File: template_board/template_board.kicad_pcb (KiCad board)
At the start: 4 copper layers, 90.2 x 95.9 mm, 123 parts, among them J1 USB_C_Receptacle_USB2.0_16P, J4 SWD, M1 MountingHole, M2 MountingHole, M3 MountingHole, M4 MountingHole, Q2 MMST3904, Q3 AO3400A, SW1 SW_Push, SW2 SW_DIP_x01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

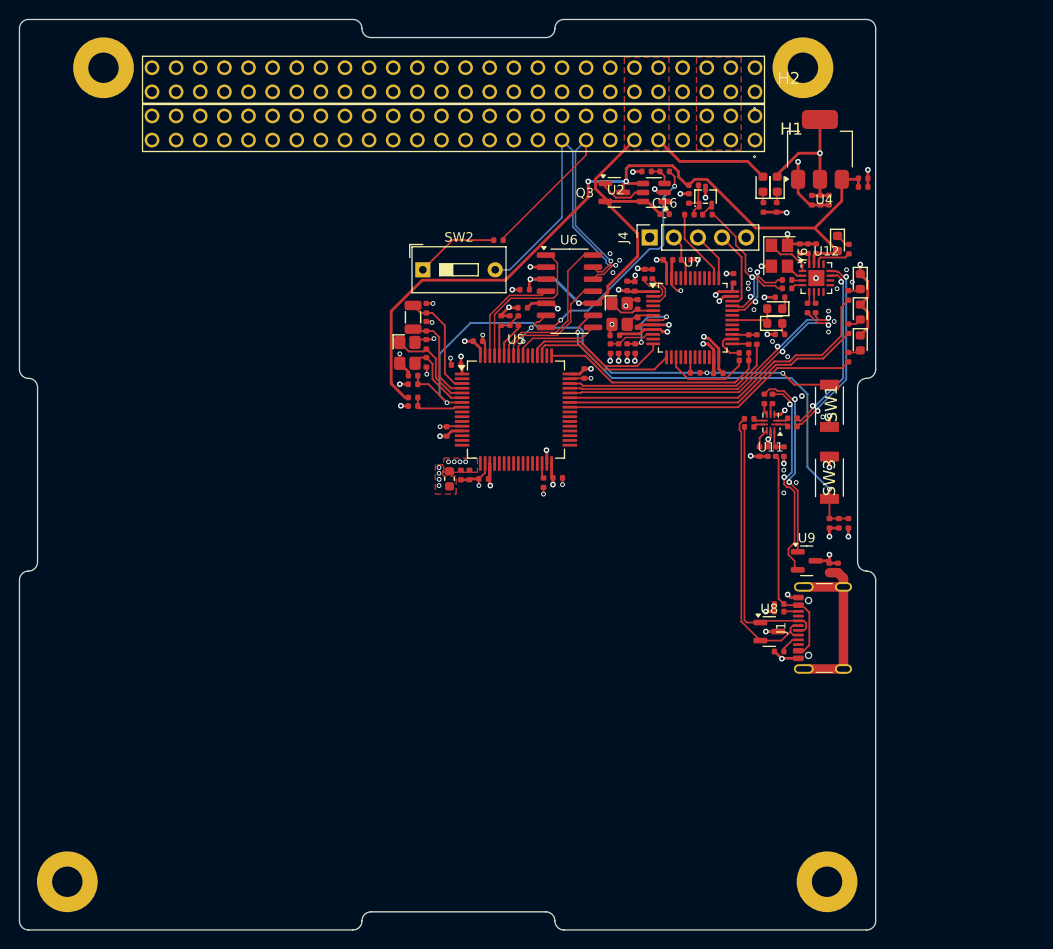
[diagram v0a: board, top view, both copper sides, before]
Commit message: [schematics] fixed issue with: stlink->crystal capacitors, usb-> esd with too big capacitance, tranzistor for stlink-usb renum changed
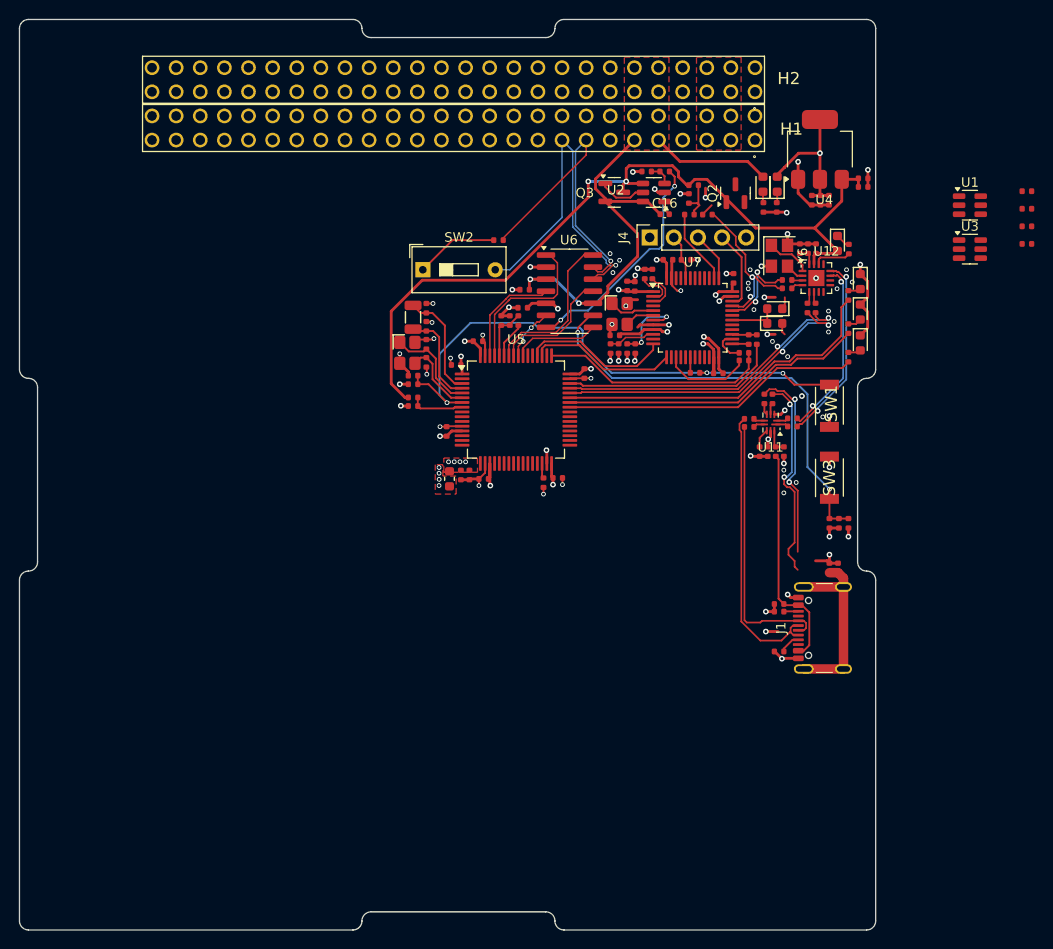
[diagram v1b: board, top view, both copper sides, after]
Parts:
- removed C8: 33pF, PCM_JLCPCB:C_0402
- removed M1, M2, M3, M4: MountingHole, MountingHole:MountingHole_3.2mm_M3_Pad
- removed R50, R51: 10kΩ, PCM_JLCPCB:R_0402
- removed U8, U9: PESD5V0S2BT, Package_TO_SOT_SMD:SOT-23
- added C19: 18pF, PCM_JLCPCB:C_0402, F.Cu at (124.3, 37.9)
- added R21: 1.2kΩ, PCM_JLCPCB:R_0402, F.Cu at (124.3, 39.7)
- added R22: 1.2kΩ, PCM_JLCPCB:R_0402, F.Cu at (124.3, 41.6)
- added U1: IP4220CZ6, Package_TO_SOT_SMD:SOT-23-6, F.Cu at (118.3, 37.5)
- added U3: IP4220CZ6, Package_TO_SOT_SMD:SOT-23-6, F.Cu at (118.3, 42.1)
- C6: value 33pF -> 18pF
- Q2: value MMST3904 -> S9013; footprint PCM_JLCPCB:Q_SOT-323 -> Package_TO_SOT_SMD:SOT-23
- moved C6 42.7 mm to (124.3, 36.0), turned to 0 degrees
- moved Q2 3.17 mm to (93.6, 36.2), turned to 90 degrees
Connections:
- C6 pad 1: /ST-LINK/STLINK-OSC_IN -> /ST-LINK/STLINK-OSC_OUT
- R17 pad 1: /USB-C/BACKPLANE.D+ -> /BUS_CONNECTOR/USB1.D+
- R18 pad 1: /USB-C/BACKPLANE.D- -> /BUS_CONNECTOR/USB1.D-
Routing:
- net /USB-C/BACKPLANE.D-: track 21.8 -> 0.00 mm, vias 2 -> 0
- net /BUS_CONNECTOR/USB1.D-: track 0.00 -> 21.8 mm, vias 0 -> 2
- net /USB-C/BACKPLANE.D+: track 20.6 -> 0.00 mm, vias 2 -> 0
- net /BUS_CONNECTOR/USB1.D+: track 0.00 -> 20.6 mm, vias 0 -> 2

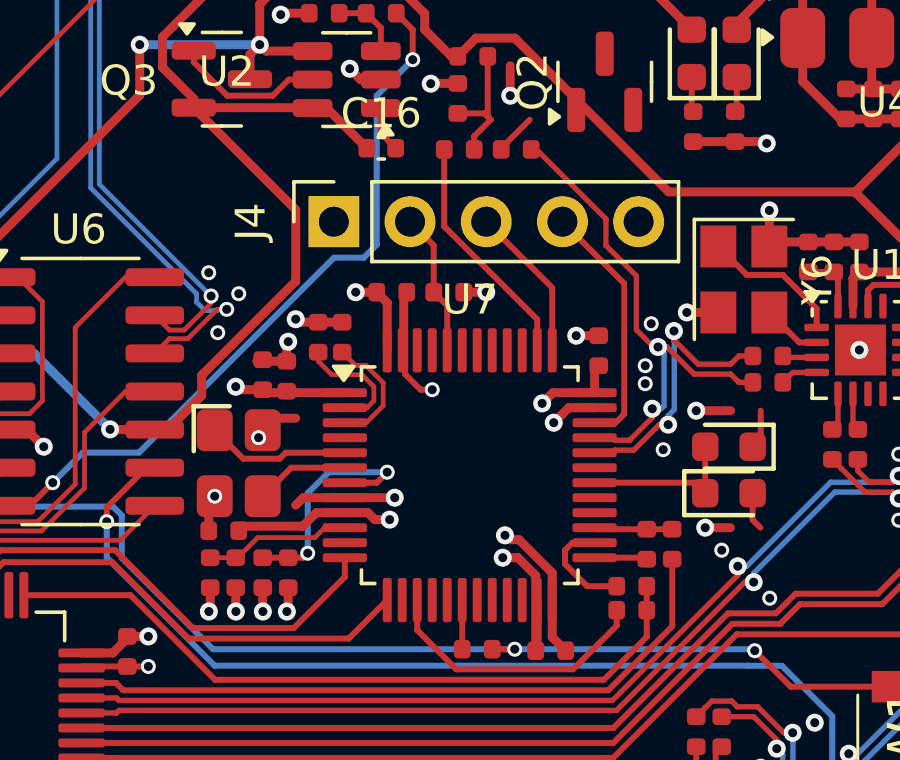
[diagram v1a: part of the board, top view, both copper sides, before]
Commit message: [schematics] changed stlink SWD pins
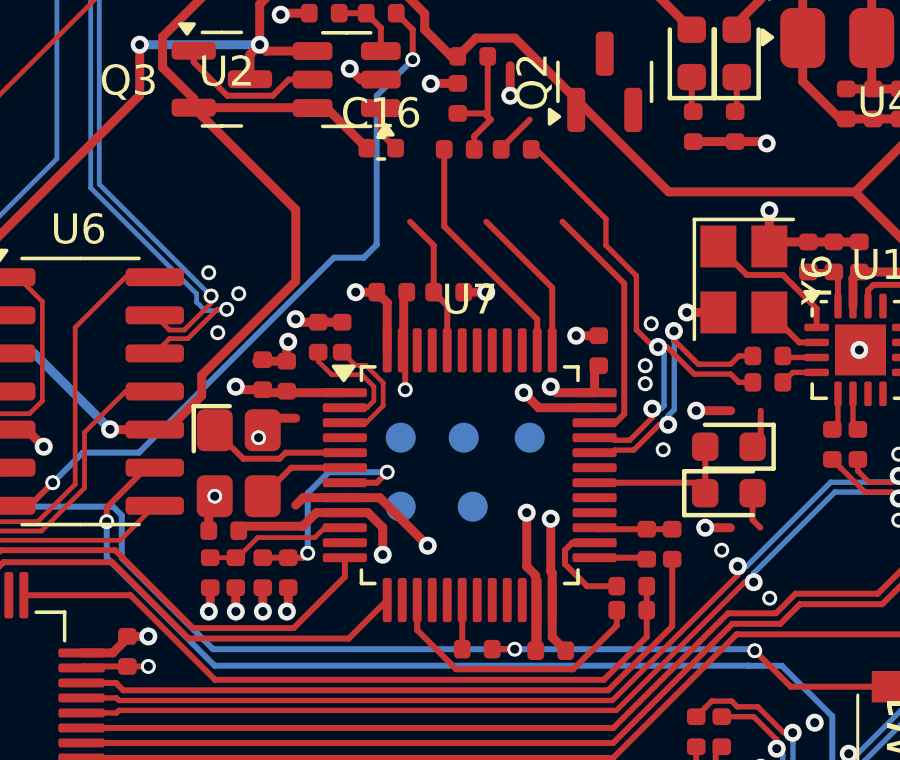
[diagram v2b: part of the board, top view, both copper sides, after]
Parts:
- removed J4: SWD, Connector_PinSocket_2.54mm:PinSocket_1x05_P2.54mm_Vertical
- added TP1: ~, TestPoint:TestPoint_Pad_D1.0mm, B.Cu at (89.2, 50.4)
- added TP2: ~, TestPoint:TestPoint_Pad_D1.0mm, B.Cu at (86.8, 50.4)
- added TP3: ~, TestPoint:TestPoint_Pad_D1.0mm, B.Cu at (88.9, 48.1)
- added TP4: ~, TestPoint:TestPoint_Pad_D1.0mm, B.Cu at (91.1, 48.1)
- added TP5: ~, TestPoint:TestPoint_Pad_D1.0mm, B.Cu at (86.8, 48.1)
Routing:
- net GND: track 102.2 -> 105.3 mm

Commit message: [schematics] complete lora board
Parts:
- added ?: , , F.Cu at (23.2, 108.8)
- added ?: , , F.Cu at (100.7, 23.1)
- added C20: 100nF, PCM_JLCPCB:C_0402, F.Cu at (72.0, 90.5)
- added C8: 22uF, PCM_JLCPCB:C_0603, F.Cu at (71.5, 89.3)
- added G***: LOGO, LOGO, F.Cu at (40.5, 103.7)
- added J2: Conn_Coaxial, Connector_Coaxial:SMA_Molex_73251-2200_Horizontal, F.Cu at (90.1, 99.3)
- added M1: MountingHole, MountingHole:MountingHole_3.2mm_M3_Pad, F.Cu at (27.0, 23.1)
- added M3: MountingHole, MountingHole:MountingHole_3.2mm_M3_Pad, F.Cu at (103.2, 108.8)
- added U8: Ai-Thinker-Ra-01, RF_Module:Ai-Thinker-Ra-01-LoRa, F.Cu at (82.6, 83.9)
- moved U3 44.8 mm to (73.9, 36.3)
- moved C6 43.1 mm to (83.4, 49.6), turned to -90 degrees
- moved C19 42.1 mm to (83.4, 47.7), turned to 90 degrees
- moved U1 37.9 mm to (97.3, 69.0), turned to 90 degrees
- moved R21 27.0 mm to (99.7, 50.8), turned to 90 degrees
- moved R22 25.7 mm to (99.7, 48.9), turned to -90 degrees
- moved TP2 5.46 mm to (85.5, 45.1), turned to 180 degrees
- moved TP5 4.03 mm to (88.8, 51.6), turned to 180 degrees
- moved TP1 2.95 mm to (86.5, 51.6), turned to 180 degrees
- moved TP3 2.13 mm to (90.5, 46.7), turned to 180 degrees
- moved Q2 1.71 mm to (91.9, 36.0)
- moved R52 1.15 mm to (91.2, 39.5)
- moved R55 1.15 mm to (89.3, 39.5)
- moved TP4 1.00 mm to (90.5, 48.9), turned to 180 degrees
- moved U4 0.29 mm to (102.4, 31.4)
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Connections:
- U5 pad 10: unconnected-(U5-PC2-Pad10) -> /LORA/LORA.MISO
- U5 pad 11: unconnected-(U5-PC3-Pad11) -> /BUS_CONNECTOR/GPIO8
- U5 pad 14: unconnected-(U5-PA0-Pad14) -> /BUS_CONNECTOR/GPIO16
- U5 pad 15: unconnected-(U5-PA1-Pad15) -> /BUS_CONNECTOR/GPIO24
- U5 pad 16: unconnected-(U5-PA2-Pad16) -> /BUS_CONNECTOR/GPIO1
- U5 pad 17: unconnected-(U5-PA3-Pad17) -> /BUS_CONNECTOR/GPIO9
- U5 pad 2: unconnected-(U5-PC13-Pad2) -> /BUS_CONNECTOR/GPIO0
- U5 pad 20: unconnected-(U5-PA4-Pad20) -> /BUS_CONNECTOR/GPIO17
- U5 pad 21: unconnected-(U5-PA5-Pad21) -> /LORA/LORA_DIO0
- U5 pad 22: unconnected-(U5-PA6-Pad22) -> /LORA/LORA_DIO1
- U5 pad 23: unconnected-(U5-PA7-Pad23) -> /LORA/LORA_DIO2
- U5 pad 24: unconnected-(U5-PC4-Pad24) -> /LORA/LORA_DIO3
- U5 pad 25: unconnected-(U5-PC5-Pad25) -> /LORA/LORA_DIO4
- U5 pad 26: unconnected-(U5-PB0-Pad26) -> /LORA/LORA_DIO5
- U5 pad 27: unconnected-(U5-PB1-Pad27) -> /LORA/LORA.CS
- U5 pad 28: unconnected-(U5-PB2-Pad28) -> /LORA/~{LORA_RESET}
- U5 pad 29: unconnected-(U5-PB10-Pad29) -> /LORA/LORA.CLK
- U5 pad 33: unconnected-(U5-PB12-Pad33) -> /BUS_CONNECTOR/GPIO18
- U5 pad 34: unconnected-(U5-PB13-Pad34) -> /BUS_CONNECTOR/GPIO26
- U5 pad 35: unconnected-(U5-PB14-Pad35) -> /BUS_CONNECTOR/GPIO3
- U5 pad 36: unconnected-(U5-PB15-Pad36) -> /BUS_CONNECTOR/GPIO11
- U5 pad 37: unconnected-(U5-PC6-Pad37) -> /BUS_CONNECTOR/GPIO19
- U5 pad 38: unconnected-(U5-PC7-Pad38) -> /BUS_CONNECTOR/GPIO27
- U5 pad 39: unconnected-(U5-PC8-Pad39) -> /BUS_CONNECTOR/GPIO4
- U5 pad 40: unconnected-(U5-PC9-Pad40) -> /BUS_CONNECTOR/GPIO12
- U5 pad 50: unconnected-(U5-PA15-Pad50) -> /BUS_CONNECTOR/GPIO10
- U5 pad 53: unconnected-(U5-PC12-Pad53) -> /BUS_CONNECTOR/GPIO2
- U5 pad 54: unconnected-(U5-PD2-Pad54) -> /BUS_CONNECTOR/GPIO25
- U5 pad 9: unconnected-(U5-PC1-Pad9) -> /LORA/LORA.MOSI
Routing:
- net /BUS_CONNECTOR/GPIO27: track 0.00 -> 105.0 mm, vias 0 -> 2
- net /BUS_CONNECTOR/GPIO12: track 0.00 -> 102.8 mm, vias 0 -> 1
- net /BUS_CONNECTOR/GPIO19: track 0.00 -> 99.0 mm, vias 0 -> 1
- net /BUS_CONNECTOR/GPIO4: track 0.00 -> 97.6 mm, vias 0 -> 1
- net /BUS_CONNECTOR/GPIO26: track 0.00 -> 95.3 mm, vias 0 -> 2
- net /BUS_CONNECTOR/GPIO11: track 0.00 -> 94.3 mm, vias 0 -> 1
- net /BUS_CONNECTOR/GPIO3: track 0.00 -> 89.0 mm, vias 0 -> 1
- net /BUS_CONNECTOR/GPIO18: track 0.00 -> 84.3 mm, vias 0 -> 1
- net /BUS_CONNECTOR/GPIO25: track 0.00 -> 70.7 mm, vias 0 -> 2
- net /BUS_CONNECTOR/GPIO10: track 0.00 -> 70.0 mm, vias 0 -> 1
- net /BUS_CONNECTOR/GPIO2: track 0.00 -> 64.3 mm, vias 0 -> 1
- net /BUS_CONNECTOR/GPIO17: track 0.00 -> 53.6 mm, vias 0 -> 1
- net /BUS_CONNECTOR/GPIO24: track 0.00 -> 50.9 mm, vias 0 -> 2
- net /BUS_CONNECTOR/GPIO16: track 0.00 -> 47.4 mm, vias 0 -> 1
- net /BUS_CONNECTOR/GPIO9: track 0.00 -> 47.4 mm, vias 0 -> 1
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
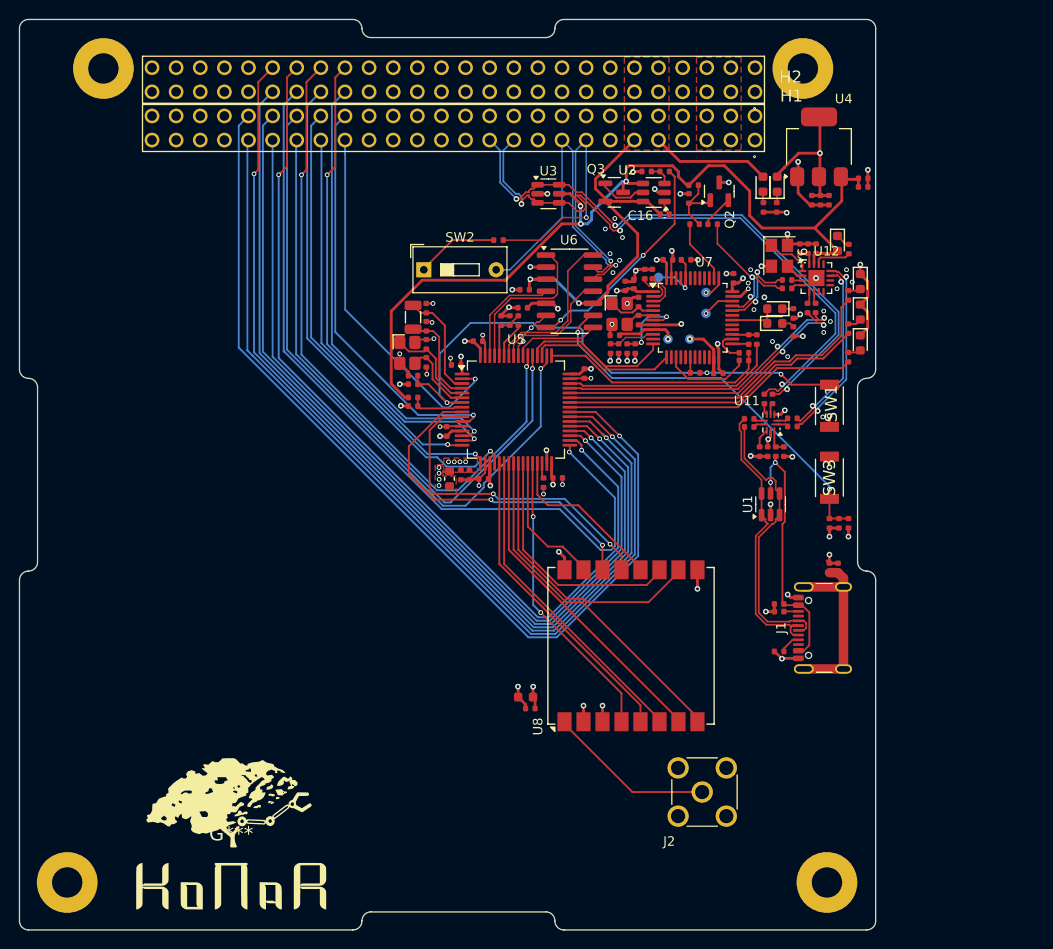
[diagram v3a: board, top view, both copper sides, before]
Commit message: fixed USB\Power leyout , added proper RF rules adn paths
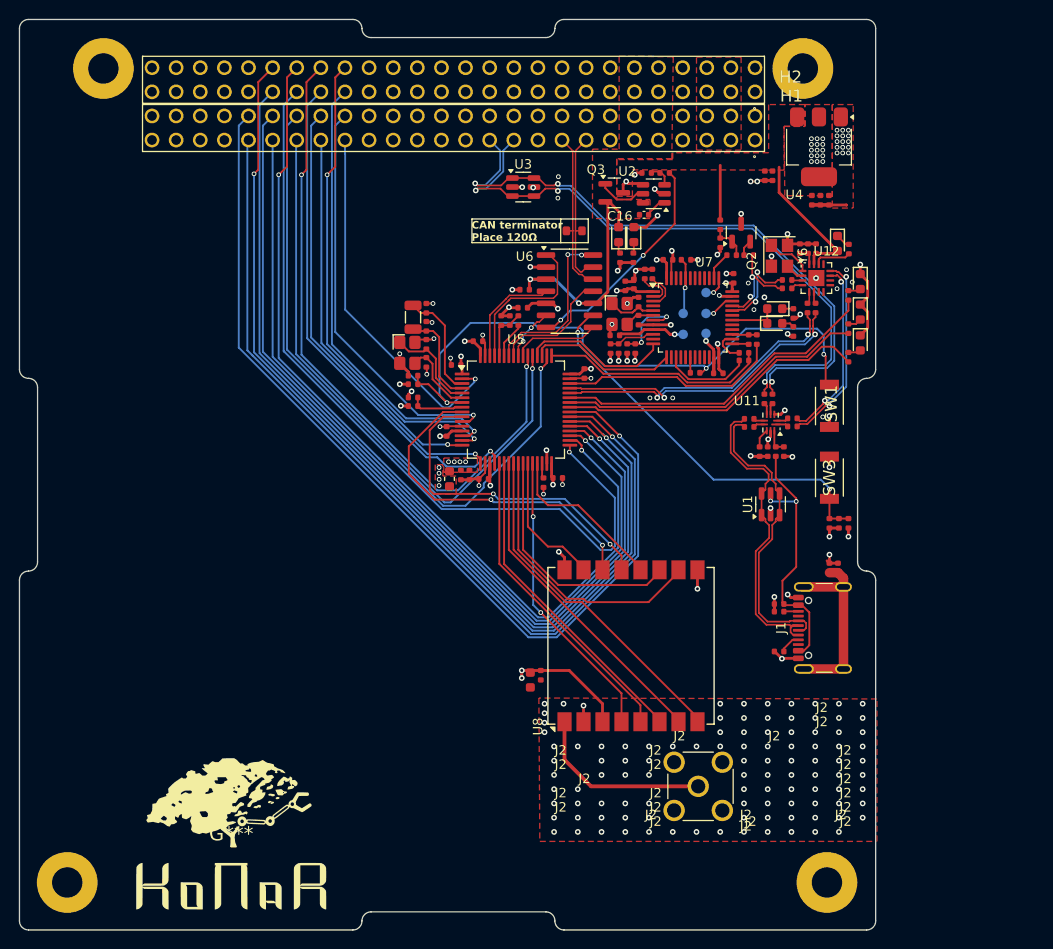
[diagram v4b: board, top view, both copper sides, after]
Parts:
- removed R2: 120Ω, PCM_JLCPCB:R_0402
- removed SW2: SW_DIP_x01, Button_Switch_THT:SW_DIP_SPSTx01_Slide_9.78x4.72mm_W7.62mm_P2.54mm
- added R24: 120Ω, PCM_JLCPCB:R_0603, F.Cu at (76.6, 40.2)
- moved D1 16.1 mm to (81.3, 40.6)
- moved R62 16.0 mm to (82.8, 43.0)
- moved D10 16.0 mm to (82.9, 40.6)
- moved R1 16.0 mm to (81.5, 43.0)
- moved C12 10.4 mm to (96.7, 34.4), turned to -90 degrees
- moved C11 9.55 mm to (97.5, 34.4), turned to -90 degrees
- moved R54 5.72 mm to (92.0, 41.5), turned to -90 degrees
- moved R55 5.08 mm to (93.2, 42.8)
- moved R53 5.02 mm to (92.0, 39.6), turned to -90 degrees
- moved R52 5.01 mm to (95.0, 42.8)
- moved Q2 4.93 mm to (94.2, 40.4)
- moved TP2 4.60 mm to (88.1, 48.9)
- moved C20 3.67 mm to (73.1, 87.0), turned to -90 degrees
- moved U3 2.74 mm to (71.2, 35.6)
- moved C16 2.18 mm to (84.0, 38.5)
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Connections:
- net Net-(J2-In) renamed /LORA/RF
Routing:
- net +5V_unprotected: track 52.4 -> 25.7 mm
- net +5V: track 92.0 -> 69.7 mm
- net /BUS_CONNECTOR/CAN1.-: track 36.5 -> 17.2 mm, vias 1 -> 0
- net /BUS_CONNECTOR/CAN1.+: track 35.3 -> 16.8 mm, vias 2 -> 0
- net Net-(R2-Pad2): track 8.76 -> 0.00 mm
- net /MCU/SWD.~{RST}: track 58.7 -> 65.1 mm
- net GND: track 111.7 -> 105.5 mm, vias 73 -> 182
- net /BUS_CONNECTOR/USB1.D-: track 60.6 -> 66.4 mm
- net /ST-LINK/ST-LINK.D+: track 15.9 -> 11.1 mm
- net /ST-LINK/USB_RENUM: track 6.74 -> 2.98 mm
- net Net-(Q2-B): track 7.36 -> 3.92 mm
- net +3V3: track 50.8 -> 47.8 mm, vias 21 -> 36
- net /USB-C/USB2S.D-: track 30.5 -> 33.5 mm
- net /USB-C/USB2S.D+: track 29.8 -> 31.7 mm
- net /BUS_CONNECTOR/USB1.D+: track 64.5 -> 66.4 mm
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- added copper zone on F.Cu, net +5V
- added copper zone on F.Cu, net GND
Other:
- board text added: "CAN terminator Place 120Ω"
- board text added: "J2"
